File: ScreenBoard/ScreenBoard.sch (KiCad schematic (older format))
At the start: 21 parts, among them J3 Conn_01x09_Male, K1 K_0051, U1 U_0076

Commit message: fix: change screen connector footprint and adjust its mechanical position
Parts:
- D9: footprint Diode_SMD:D_SOD-523 -> Diode_SMD:D_SOD-128
- J3: footprint Connector_PinHeader_1.27mm:PinHeader_1x09_P1.27mm_Vertical -> Connector_PinHeader_2.00mm:PinHeader_1x09_P2.00mm_Vertical
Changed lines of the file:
@@
 $EndDescr
-$Comp
-L VESC_UI-rescue:K_0051-DVB_K-DK3_GUI-PI-rescue K1
-U 1 1 5CB72034
-P 5200 4100
-F 0 "K1" H 5145 4822 39  0000 C CNN
-F 1 "K_0051" H 5200 3600 39  0001 C CNN
-F 2 "SamacSys_Parts:52435-3071" H 5200 3500 39  0001 C CNN
-F 3 "http://www.farnell.com/datasheets/1875032.pdf?_ga=2.157046779.1318262782.1499092899-695518372.1495123464" H 5200 3400 39  0001 C CNN
-F 4 "52435-3071" H 5145 4724 39  0000 C CNN "Field4"
-F 5 "30p" H 5200 3300 39  0001 C CNN "Field5"
-F 6 "fem" H 5200 3200 39  0001 C CNN "Field6"
-F 7 "RA" H 5200 3100 39  0001 C CNN "Field7"
-	1    5200 4100
-	1    0    0    -1
-$EndComp
 $Comp
 L VESC_UI-rescue:C_0003-DVB_C C1
@@
 F 0 "D9" H 5300 1434 39  0000 C CNN
 F 1 "D_0021" H 5300 1450 39  0001 C CNN
-F 2 "Diode_SMD:D_SOD-523" H 5300 1375 39  0001 C CNN
+F 2 "Diode_SMD:D_SOD-128" H 5300 1375 39  0001 C CNN
 F 3 "http://www.farnell.com/datasheets/2304408.pdf?_ga=2.70745296.1318262782.1499092899-695518372.1495123464" H 5300 1300 39  0001 C CNN
 F 4 "MBR0530" H 5300 1525 39  0000 C CNN "Field4"
@@
 F 0 "J3" H 10350 850 39  0000 C CNN
 F 1 "Conn_01x09_Male" H 10350 750 39  0001 C CNN
-F 2 "Connector_PinHeader_1.27mm:PinHeader_1x09_P1.27mm_Vertical" H 10250 1250 39  0001 C CNN
+F 2 "Connector_PinHeader_2.00mm:PinHeader_1x09_P2.00mm_Vertical" H 10250 1250 39  0001 C CNN
 F 3 "~" H 10250 1250 39  0001 C CNN
 F 4 "Main" H 10375 1775 39  0000 C CNN "Name"
@@
 Wire Wire Line
 	5450 1650 5550 1650
-Wire Wire Line
-	4600 4400 4700 4400
 NoConn ~ 6300 4400
 NoConn ~ 6400 4400
@@
 	3925 2375 3925 2075
 Connection ~ 3925 2075
-Wire Wire Line
-	5000 4400 5050 4400
-Wire Wire Line
-	4700 4400 4800 4400
-Connection ~ 4700 4400
-Wire Wire Line
-	4900 4400 4800 4400
-Connection ~ 4800 4400
 $Comp
 L Device:R R8
@@
 Wire Wire Line
 	3700 1950 3700 1975
-Wire Wire Line
-	4900 4400 5000 4400
-Connection ~ 4900 4400
-Connection ~ 5000 4400
 Text Label 5900 4400 3    39   ~ 0
 OLED_CS
@@
 	3925 1650 4400 1650
 Connection ~ 10450 950
+Connection ~ 4800 4400
+Wire Wire Line
+	4700 4400 4800 4400
+Wire Wire Line
+	4600 4400 4700 4400
+Connection ~ 4700 4400
+Wire Wire Line
+	5000 4400 5050 4400
+Connection ~ 5000 4400
+Wire Wire Line
+	4900 4400 5000 4400
+Wire Wire Line
+	4900 4400 4800 4400
+Connection ~ 4900 4400
+$Comp
+L VESC_UI-rescue:K_0051-DVB_K-DK3_GUI-PI-rescue K1
+U 1 1 5CB72034
+P 5200 4100
+F 0 "K1" H 5145 4822 39  0000 C CNN
+F 1 "K_0051" H 5200 3600 39  0001 C CNN
+F 2 "SamacSys_Parts:52435-3071" H 5200 3500 39  0001 C CNN
+F 3 "http://www.farnell.com/datasheets/1875032.pdf?_ga=2.157046779.1318262782.1499092899-695518372.1495123464" H 5200 3400 39  0001 C CNN
+F 4 "52435-3071" H 5145 4724 39  0000 C CNN "Field4"
+F 5 "30p" H 5200 3300 39  0001 C CNN "Field5"
+F 6 "fem" H 5200 3200 39  0001 C CNN "Field6"
+F 7 "RA" H 5200 3100 39  0001 C CNN "Field7"
+	1    5200 4100
+	1    0    0    -1
+$EndComp
 $EndSCHEMATC

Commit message: fix and refactor: both mainboard and screenboard
Many improvements made
- Fixed all issues with footprints
- Optimized components placement and tracks
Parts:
- D9: footprint Diode_SMD:D_SOD-128 -> Diode_SMD:D_SOD-123
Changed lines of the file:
@@
 F 0 "D9" H 5300 1434 39  0000 C CNN
 F 1 "D_0021" H 5300 1450 39  0001 C CNN
-F 2 "Diode_SMD:D_SOD-128" H 5300 1375 39  0001 C CNN
+F 2 "Diode_SMD:D_SOD-123" H 5300 1375 39  0001 C CNN
 F 3 "http://www.farnell.com/datasheets/2304408.pdf?_ga=2.70745296.1318262782.1499092899-695518372.1495123464" H 5300 1300 39  0001 C CNN
 F 4 "MBR0530" H 5300 1525 39  0000 C CNN "Field4"

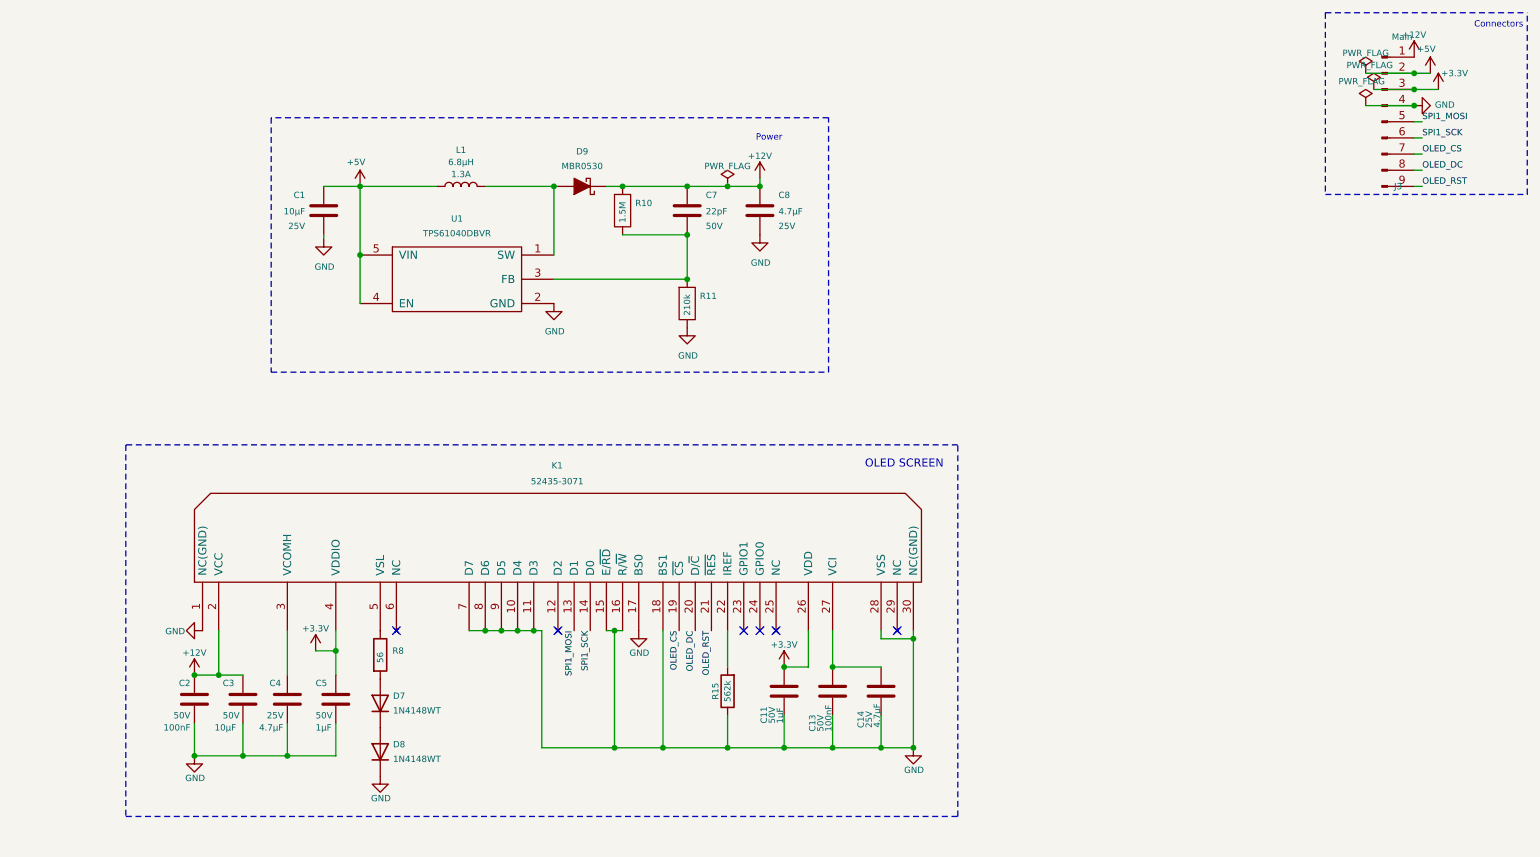
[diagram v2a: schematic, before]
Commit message: feature: change power circuit
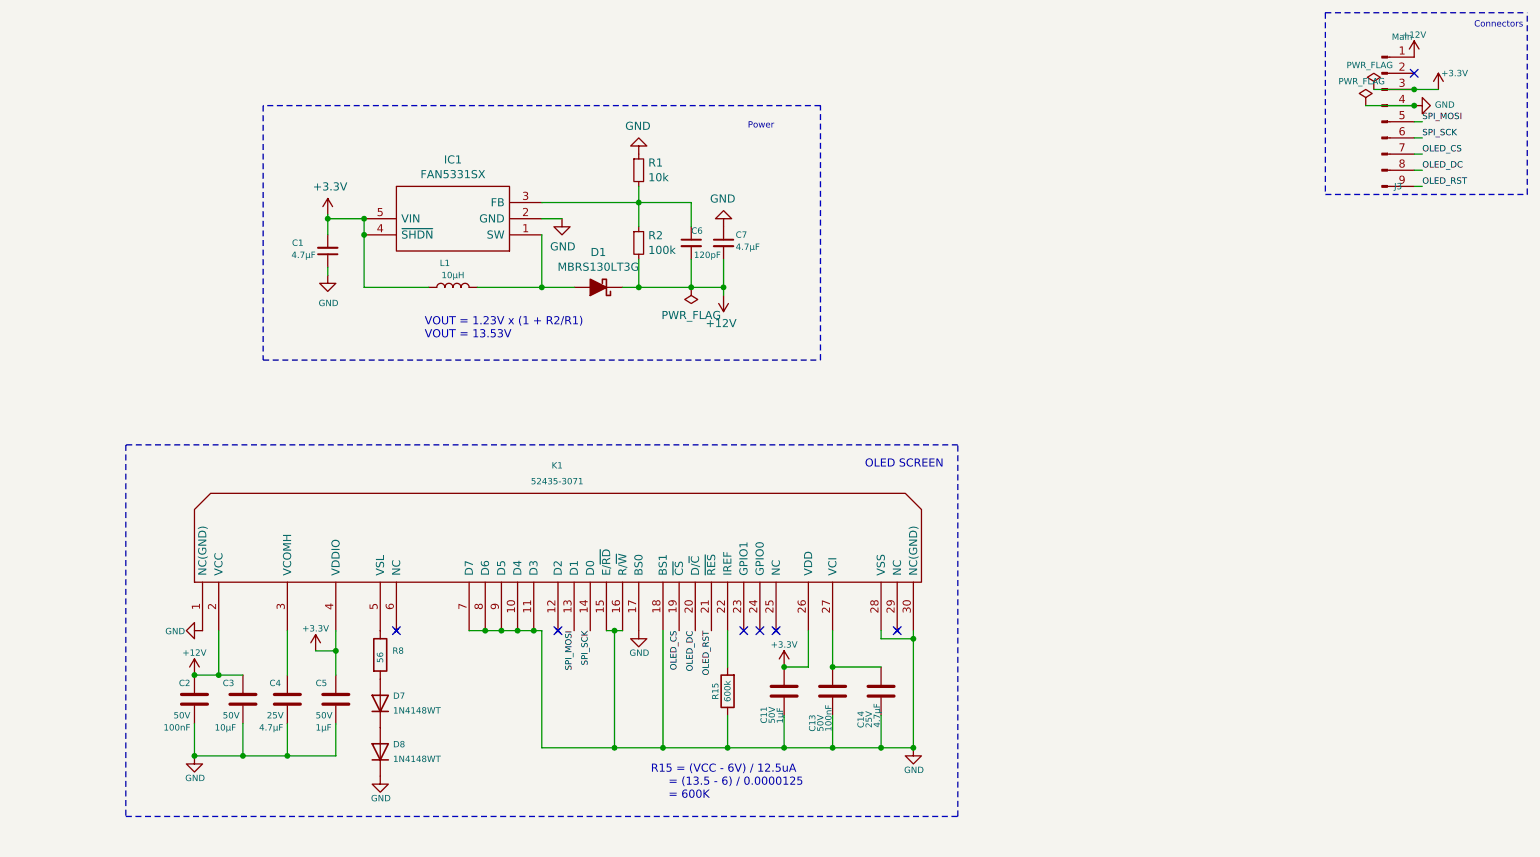
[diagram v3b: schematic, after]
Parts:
- removed C1: C_0003, Capacitor_SMD:C_0603_1608Metric_Pad1.05x0.95mm_HandSolder, symbol VESC_UI-rescue:C_0003-DVB_C
- removed C7: C_0013, Capacitor_SMD:C_0603_1608Metric_Pad1.05x0.95mm_HandSolder, symbol VESC_UI-rescue:C_0013-DVB_C
- removed C8: C_0036, Capacitor_SMD:C_0603_1608Metric_Pad1.05x0.95mm_HandSolder, symbol VESC_UI-rescue:C_0036-DVB_C
- removed D9: D_0021, Diode_SMD:D_SOD-123, symbol VESC_UI-rescue:D_0021-DVB_D
- removed R10: R_0107, Resistor_SMD:R_0603_1608Metric_Pad1.05x0.95mm_HandSolder, symbol VESC_UI-rescue:R_0107-DVB_R
- removed R11: R_0108, Resistor_SMD:R_0603_1608Metric_Pad1.05x0.95mm_HandSolder, symbol VESC_UI-rescue:R_0108-DVB_R
- removed U1: U_0076, Package_TO_SOT_SMD:SOT-23-5, symbol VESC_UI-rescue:U_0076-DVB_U
- added C1, C7: 4.7µF, Capacitor_SMD:C_0603_1608Metric_Pad1.05x0.95mm_HandSolder, symbol Device:C_Small
- added C6: 120pF, Capacitor_SMD:C_0603_1608Metric_Pad1.05x0.95mm_HandSolder, symbol Device:C_Small
- added D1: MBRS130LT3G, Diode_SMD:D_SMB_Handsoldering, symbol Device:D_Schottky_ALT
- added IC1: FAN5331SX, SOT95P280X145-5N, symbol SamacSys_Parts:FAN5331SX
- added R1: 10k, Resistor_SMD:R_0603_1608Metric_Pad1.05x0.95mm_HandSolder, symbol Device:R_Small
- added R2: 100k, Resistor_SMD:R_0603_1608Metric_Pad1.05x0.95mm_HandSolder, symbol Device:R_Small
- C11, C5: value C_0056 -> 1µF
- C13, C2: value C_0033 -> 100nF
- C14, C4: value C_0036 -> 4.7µF
- C3: value C_0041 -> 10µF
- D7, D8: value D_0022 -> 1N4148WT
- K1: value K_0051 -> OLED connector
- L1: value L_0011 -> 10µH; footprint Inductor_SMD:L_Coilcraft_LPS4018 -> Inductor_SMD:L_Coilcraft_LPS5030; Field4 LPS4018-682MRB -> LPS5030-103MRB; Field5 1.3A -> 1.4A; Field7 6.8µH -> (none)
- R15: value R_0019 -> 600k; Field4 562k -> 600k
- R8: value R_0110 -> 56 Ohm
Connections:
- net +12V: now also C6.2, C7.2, D1.1 (K), R2.2
- net +3V3: now also L1.1, C1.2, IC1.4 (~SHDN), IC1.5 (VIN)
- net GND: now also C1.1, C7.1, IC1.2 (GND), R1.1
- net at L1.2: now also D1.2 (A), IC1.1 (SW)
- net +5V: no longer names the net of J3.2 (Pin_2)
- net +5V: no longer L1.1
- net SPI1_MOSI renamed SPI_MOSI
- net SPI1_SCK renamed SPI_SCK
- new net: C6.1, IC1.3 (FB), R1.2, R2.1
- no-connect marks 6 -> 7
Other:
- note added: "R15 = (VCC - 6V) / 12.5uA\n = (13.5 - 6) / 0.0000125\n = 600K"
- note added: "VOUT = 1.23V x (1 + R2/R1)\nVOUT = 13.53V"

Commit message: Finalized PCBs
- Add MicroSD Card support on screen board
- Fix Hall sensors footprints (flip board side)
- Change screen connector
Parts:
- added C11: 10µF, Capacitor_SMD:C_0603_1608Metric_Pad1.05x0.95mm_HandSolder, symbol Device:C_Small
- added J1: Micro_SD_Card, SamacSys_Parts:693072010801, symbol Connector:Micro_SD_Card
- J2: renamed from J3; value Conn_01x09_Male -> Conn_02x05_Male; footprint Connector_PinHeader_2.00mm:PinHeader_1x09_P2.00mm_Vertical -> Connector_PinHeader_2.00mm:PinHeader_2x05_P2.00mm_Vertical_SMD; symbol Connector:Conn_01x09_Male -> Connector_Generic:Conn_02x05_Odd_Even
- renumbered C14 to C10, C11 to C8, C13 to C9, D7 to D1, D8 to D2, D1 to D3, R8 to R1, R1 to R2, R2 to R3, R15 to R4
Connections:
- net +3V3: now also J2.2 (Pin_2), C11.2, J1.4 (VDD); no longer J2.3 (Pin_3)
- net GND: now also J2.3 (Pin_3), C11.1, J1.6 (VSS), J1.9 (SHIELD); no longer J2.4 (Pin_4)
- net OLED_CS: now also J2.8 (Pin_8); no longer J2.7 (Pin_7)
- net OLED_DC: now also J2.7 (Pin_7); no longer J2.8 (Pin_8)
- net SPI_MOSI: now also J2.4 (Pin_4), J1.3 (CMD); no longer J2.5 (Pin_5)
- net SPI_SCK: now also J1.5 (CLK)
- new net SD_CS: J1.2 (DAT3/CD), J2.10 (Pin_10)
- new net SPI_MISO: J1.7 (DAT0), J2.5 (Pin_5)
- no-connect marks 7 -> 8
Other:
- note added: "MicroSD Card"
- note added: "OLED screen"
- note added: "R4 = (VCC - 6V) / 12.5uA\n = (13.5 - 6) / 0.0000125\n = 600K"
- note added: "VOUT = 1.23V x (1 + R3/R2)\nVOUT = 13.53V"
- note removed: "OLED SCREEN"
- note removed: "R15 = (VCC - 6V) / 12.5uA\n = (13.5 - 6) / 0.0000125\n = 600K"
- note removed: "VOUT = 1.23V x (1 + R2/R1)\nVOUT = 13.53V"
- moved on the sheet: C1, C10, C2, C3, C4, C5, C6, C7, C8, C9, D1, D2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

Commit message: Change C11 footprint for better component availability
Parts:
- C10, C2, C3, C4, C5, C8, C9: symbol Device:C -> Device:C_Small
- C11: footprint Capacitor_SMD:C_0603_1608Metric_Pad1.05x0.95mm_HandSolder -> Capacitor_SMD:C_1206_3216Metric_Pad1.42x1.75mm_HandSolder
- L1: symbol Device:L -> Device:L_Small
- R1, R4: symbol Device:R -> Device:R_Small
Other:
- moved on the sheet: C2, C3, C4, C5, D1, D2, R1
